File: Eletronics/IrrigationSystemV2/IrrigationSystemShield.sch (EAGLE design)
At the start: 51 parts, among them T1-THERM2 THERMISTOR-2,5, U1 ARDUINO-MEGANOSILK, U1-SOL1 RELAY-SOLIDSTATEPTH, U1-SOL2 RELAY-SOLIDSTATEPTH

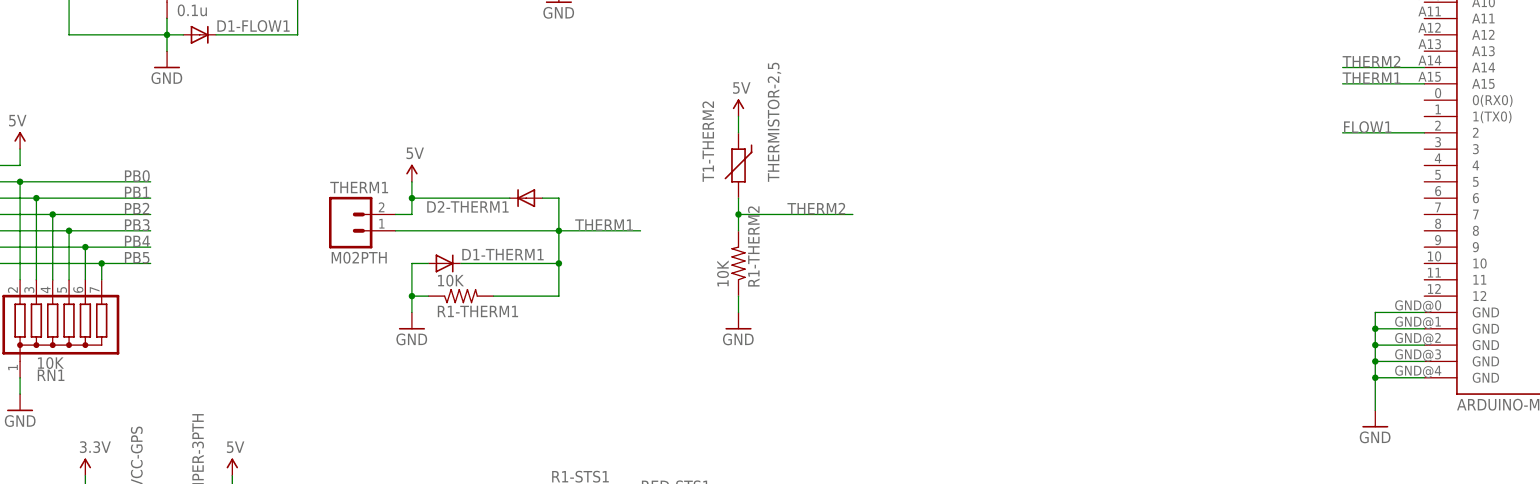
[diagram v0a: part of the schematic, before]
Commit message: Added ability to add Interrupt to PB5.
Updated Schematic to include interrupt. Need to run trace for
interrupt. If trace is not run PB5 will still work as a non interrupted
pin.
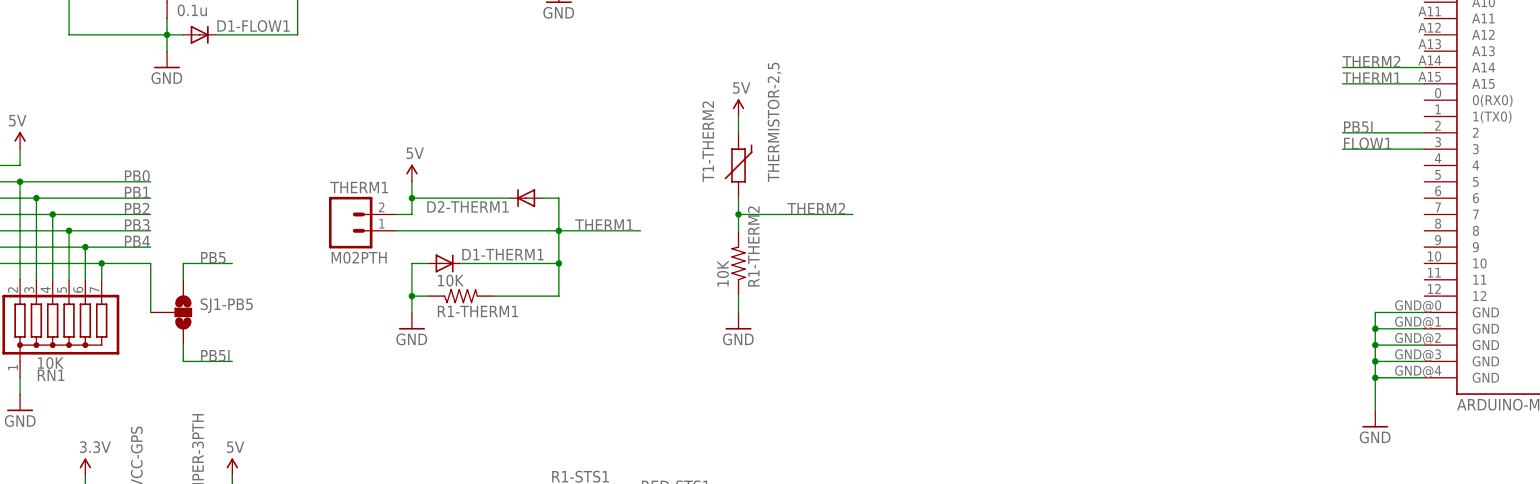
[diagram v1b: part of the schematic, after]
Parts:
- added SJ1-PB5: (no value), SparkFun-Passives:SOLDERJUMPER_2WAYS
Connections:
- new net PB5I: SJ1-PB5.3, U1.2
- new net PB5RAW: BUTTONS.7, RN1.7, SJ1-PB5.2
- net FLOW1: now also U1.3; no longer U1.2
- net PB5: now also SJ1-PB5.1; no longer BUTTONS.7, RN1.7
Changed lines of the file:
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@@
 <grid distance="0.1" unitdist="inch" unit="inch" style="lines" multiple="1" display="no" altdistance="0.01" altunitdist="inch" altunit="inch"/>
 <layers>
-<layer number="1" name="Top" color="4" fill="1" visible="yes" active="no"/>
-<layer number="16" name="Bottom" color="1" fill="1" visible="yes" active="no"/>
-<layer number="17" name="Pads" color="2" fill="1" visible="yes" active="no"/>
-<layer number="18" name="Vias" color="2" fill="1" visible="yes" active="no"/>
-<layer number="19" name="Unrouted" color="6" fill="1" visible="yes" active="no"/>
-<layer number="20" name="Dimension" color="15" fill="1" visible="yes" active="no"/>
-<layer number="21" name="tPlace" color="14" fill="1" visible="yes" active="no"/>
-<layer number="22" name="bPlace" color="7" fill="1" visible="yes" active="no"/>
-<layer number="23" name="tOrigins" color="15" fill="1" visible="yes" active="no"/>
-<layer number="24" name="bOrigins" color="15" fill="1" visible="yes" active="no"/>
-<layer number="25" name="tNames" color="7" fill="1" visible="yes" active="no"/>
-<layer number="26" name="bNames" color="7" fill="1" visible="yes" active="no"/>
-<layer number="27" name="tValues" color="7" fill="1" visible="yes" active="no"/>
-<layer number="28" name="bValues" color="7" fill="1" visible="yes" active="no"/>
+<layer number="1" name="Top" color="4" fill="1" visible="no" active="no"/>
+<layer number="16" name="Bottom" color="1" fill="1" visible="no" active="no"/>
+<layer number="17" name="Pads" color="2" fill="1" visible="no" active="no"/>
+<layer number="18" name="Vias" color="2" fill="1" visible="no" active="no"/>
+<layer number="19" name="Unrouted" color="6" fill="1" visible="no" active="no"/>
+<layer number="20" name="Dimension" color="15" fill="1" visible="no" active="no"/>
+<layer number="21" name="tPlace" color="14" fill="1" visible="no" active="no"/>
+<layer number="22" name="bPlace" color="7" fill="1" visible="no" active="no"/>
+<layer number="23" name="tOrigins" color="15" fill="1" visible="no" active="no"/>
+<layer number="24" name="bOrigins" color="15" fill="1" visible="no" active="no"/>
+<layer number="25" name="tNames" color="7" fill="1" visible="no" active="no"/>
+<layer number="26" name="bNames" color="7" fill="1" visible="no" active="no"/>
+<layer number="27" name="tValues" color="7" fill="1" visible="no" active="no"/>
+<layer number="28" name="bValues" color="7" fill="1" visible="no" active="no"/>
 <layer number="29" name="tStop" color="7" fill="3" visible="no" active="no"/>
 <layer number="30" name="bStop" color="7" fill="6" visible="no" active="no"/>
@@
 <layer number="35" name="tGlue" color="7" fill="4" visible="no" active="no"/>
 <layer number="36" name="bGlue" color="7" fill="5" visible="no" active="no"/>
-<layer number="37" name="tTest" color="7" fill="1" visible="yes" active="no"/>
-<layer number="38" name="bTest" color="7" fill="1" visible="yes" active="no"/>
+<layer number="37" name="tTest" color="7" fill="1" visible="no" active="no"/>
+<layer number="38" name="bTest" color="7" fill="1" visible="no" active="no"/>
 <layer number="39" name="tKeepout" color="4" fill="11" visible="no" active="no"/>
 <layer number="40" name="bKeepout" color="1" fill="11" visible="no" active="no"/>
@@
 <layer number="44" name="Drills" color="7" fill="1" visible="no" active="no"/>
 <layer number="45" name="Holes" color="7" fill="1" visible="no" active="no"/>
-<layer number="46" name="Milling" color="3" fill="1" visible="yes" active="no"/>
-<layer number="47" name="Measures" color="7" fill="1" visible="yes" active="no"/>
-<layer number="48" name="Document" color="7" fill="1" visible="yes" active="no"/>
-<layer number="49" name="Reference" color="7" fill="1" visible="yes" active="no"/>
-<layer number="50" name="dxf" color="7" fill="1" visible="yes" active="no"/>
-<layer number="51" name="tDocu" color="7" fill="1" visible="yes" active="no"/>
-<layer number="52" name="bDocu" color="7" fill="1" visible="yes" active="no"/>
-<layer number="53" name="tGND_GNDA" color="7" fill="9" visible="yes" active="no"/>
-<layer number="54" name="bGND_GNDA" color="1" fill="9" visible="yes" active="no"/>
-<layer number="56" name="wert" color="7" fill="1" visible="yes" active="no"/>
+<layer number="46" name="Milling" color="3" fill="1" visible="no" active="no"/>
+<layer number="47" name="Measures" color="7" fill="1" visible="no" active="no"/>
+<layer number="48" name="Document" color="7" fill="1" visible="no" active="no"/>
+<layer number="49" name="Reference" color="7" fill="1" visible="no" active="no"/>
+<layer number="50" name="dxf" color="7" fill="1" visible="no" active="no"/>
+<layer number="51" name="tDocu" color="7" fill="1" visible="no" active="no"/>
+<layer number="52" name="bDocu" color="7" fill="1" visible="no" active="no"/>
+<layer number="53" name="tGND_GNDA" color="7" fill="9" visible="no" active="no"/>
+<layer number="54" name="bGND_GNDA" color="1" fill="9" visible="no" active="no"/>
+<layer number="56" name="wert" color="7" fill="1" visible="no" active="no"/>
 <layer number="91" name="Nets" color="2" fill="1" visible="yes" active="yes"/>
 <layer number="92" name="Busses" color="1" fill="1" visible="yes" active="yes"/>
@@
 <part name="GND13" library="SparkFun-Aesthetics" deviceset="GND" device=""/>
 <part name="STS1" library="Library" deviceset="LED-RGB-CC-THRU" device="DIFFUSE"/>
+<part name="SJ1-PB5" library="SparkFun-Passives" deviceset="SOLDERJUMPER_2WAY" device="S"/>
 </parts>
 <sheets>
@@
 <instance part="GND13" gate="1" x="104.14" y="88.9"/>
 <instance part="STS1" gate="G$1" x="116.84" y="99.06" rot="MR0"/>
+<instance part="SJ1-PB5" gate="G$1" x="71.12" y="134.62"/>
 </instances>
 <busses>
@@
 </segment>
 <segment>
-<pinref part="U1" gate="G$1" pin="2"/>
-<wire x1="264.16" y1="162.56" x2="251.46" y2="162.56" width="0.1524" layer="91"/>
-<label x="251.46" y="162.56" size="1.778" layer="95"/>
+<pinref part="U1" gate="G$1" pin="3"/>
+<wire x1="264.16" y1="160.02" x2="251.46" y2="160.02" width="0.1524" layer="91"/>
+<label x="251.46" y="160.02" size="1.778" layer="95"/>
 </segment>
 </net>
@@
 <net name="PB5" class="0">
 <segment>
-<wire x1="40.64" y1="142.24" x2="58.42" y2="142.24" width="0.1524" layer="91"/>
-<label x="66.04" y="142.24" size="1.778" layer="95" rot="MR0"/>
-<pinref part="BUTTONS" gate="G$1" pin="7"/>
-<pinref part="RN1" gate="G$1" pin="7"/>
-<wire x1="58.42" y1="142.24" x2="66.04" y2="142.24" width="0.1524" layer="91"/>
-<wire x1="58.42" y1="139.7" x2="58.42" y2="142.24" width="0.1524" layer="91"/>
-<junction x="58.42" y="142.24"/>
-</segment>
-<segment>
 <pinref part="U1" gate="G$1" pin="41"/>
 <wire x1="304.8" y1="154.94" x2="312.42" y2="154.94" width="0.1524" layer="91"/>
 <label x="307.34" y="154.94" size="1.778" layer="95"/>
+</segment>
+<segment>
+<pinref part="SJ1-PB5" gate="G$1" pin="1"/>
+<wire x1="71.12" y1="139.7" x2="71.12" y2="142.24" width="0.1524" layer="91"/>
+<wire x1="71.12" y1="142.24" x2="78.74" y2="142.24" width="0.1524" layer="91"/>
+<label x="73.66" y="142.24" size="1.778" layer="95"/>
 </segment>
 </net>
@@
 </segment>
 </net>
+<net name="PB5RAW" class="0">
+<segment>
+<wire x1="40.64" y1="142.24" x2="58.42" y2="142.24" width="0.1524" layer="91"/>
+<pinref part="BUTTONS" gate="G$1" pin="7"/>
+<pinref part="RN1" gate="G$1" pin="7"/>
+<wire x1="58.42" y1="139.7" x2="58.42" y2="142.24" width="0.1524" layer="91"/>
+<wire x1="58.42" y1="142.24" x2="66.04" y2="142.24" width="0.1524" layer="91"/>
+<junction x="58.42" y="142.24"/>
+<pinref part="SJ1-PB5" gate="G$1" pin="2"/>
+<wire x1="66.04" y1="142.24" x2="66.04" y2="134.62" width="0.1524" layer="91"/>
+</segment>
+</net>
+<net name="PB5I" class="0">
+<segment>
+<pinref part="SJ1-PB5" gate="G$1" pin="3"/>
+<wire x1="71.12" y1="129.54" x2="71.12" y2="127" width="0.1524" layer="91"/>
+<wire x1="71.12" y1="127" x2="78.74" y2="127" width="0.1524" layer="91"/>
+<label x="73.66" y="127" size="1.778" layer="95"/>
+</segment>
+<segment>
+<pinref part="U1" gate="G$1" pin="2"/>
+<wire x1="264.16" y1="162.56" x2="251.46" y2="162.56" width="0.1524" layer="91"/>
+<label x="251.46" y="162.56" size="1.778" layer="95"/>
+</segment>
+</net>
